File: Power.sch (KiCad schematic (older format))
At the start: 31 parts, among them J10 FAN, J8 PWR, Q1 AOD4189, Q10 MMBT3904, Q11 IRFML8244, Q2 AOD4189, Q8 MMBT3904, Q9 MMBT3906

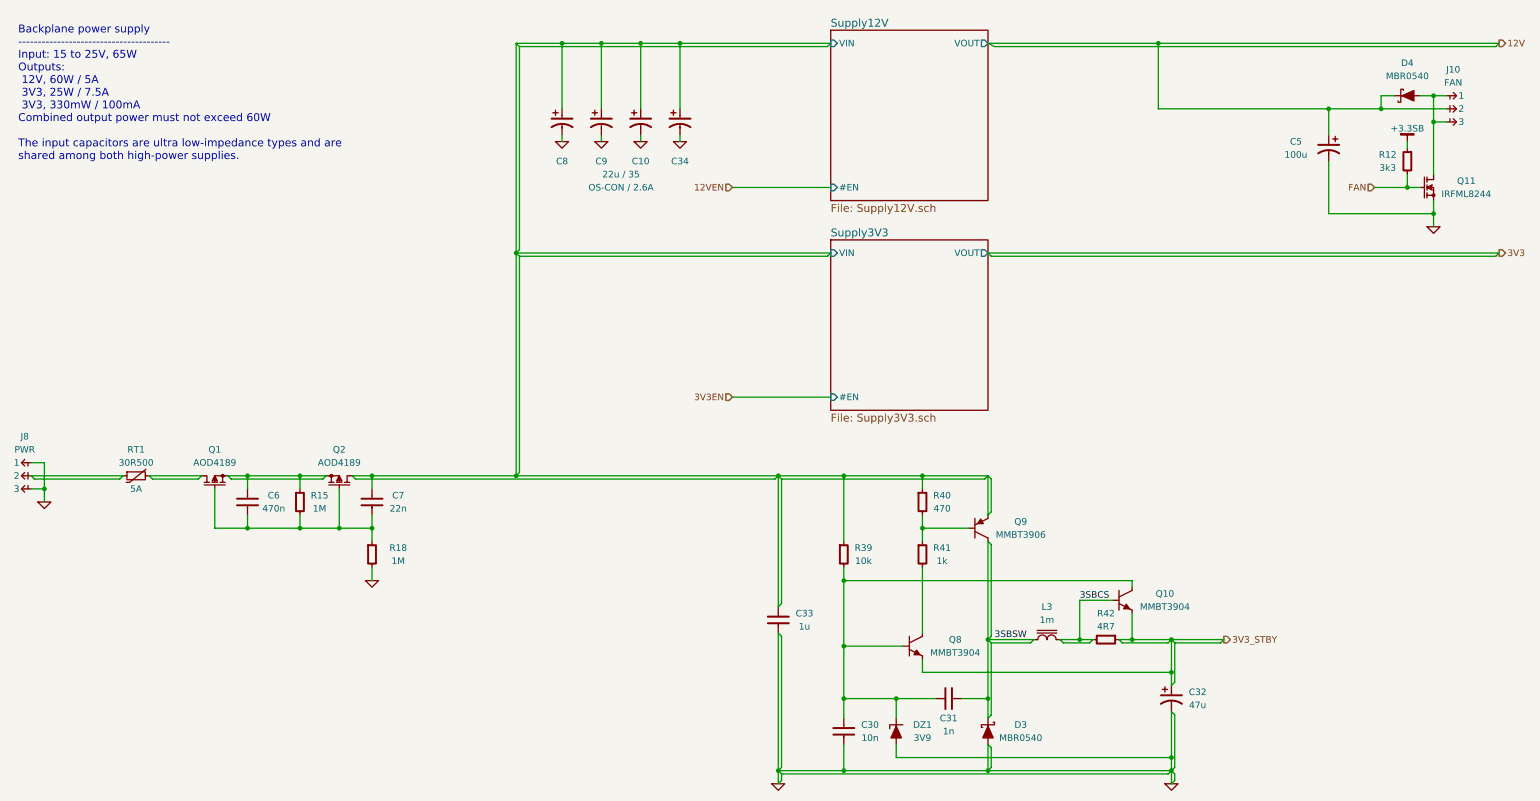
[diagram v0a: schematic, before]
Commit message: Reannotated parts
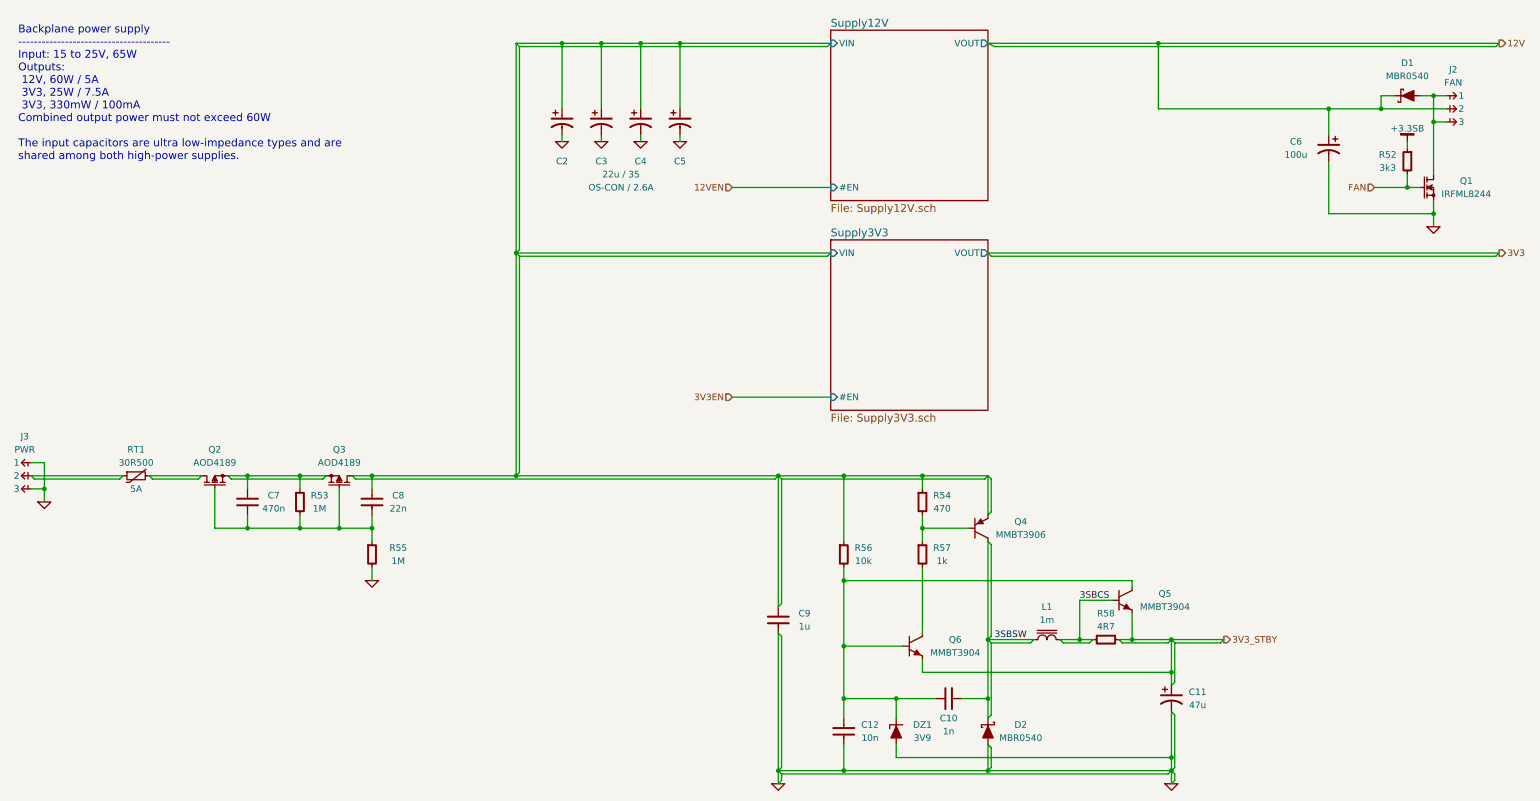
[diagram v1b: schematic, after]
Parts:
- renumbered C31 to C10, C32 to C11, C30 to C12, C8 to C2, C9 to C3, C10 to C4, C34 to C5, C5 to C6, C6 to C7, C7 to C8, C33 to C9, D4 to D1, D3 to D2, J10 to J2, J8 to J3, L3 to L1, Q11 to Q1, Q1 to Q2, Q2 to Q3, Q9 to Q4, Q10 to Q5, Q8 to Q6, R12 to R52, R15 to R53, R40 to R54, R18 to R55, R39 to R56, R41 to R57, R42 to R58

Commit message: Silkscreen and 3D touchups
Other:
- moved on the sheet: C10, C11, C12, C2, C3, C4, C5, C6, C7, C8, C9, D1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

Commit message: Changed BSS138 to MMUN221
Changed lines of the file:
@@
 $EndComp
 Wire Wire Line
-	7500 4600 7500 5350
-Wire Wire Line
-	7500 5350 7500 5800
-Wire Wire Line
-	7500 5800 7500 5950
+	7500 4600 7500 5950
 Wire Wire Line
 	7500 5350 7850 5350
@@
 	7350 4500 7000 4500
 Wire Wire Line
-	7000 4400 7000 4500
-Wire Wire Line
-	7000 4500 7000 4600
+	7000 4400 7000 4600
 Connection ~ 7000 4500
 Wire Wire Line
-	8050 5350 8200 5350
-Wire Wire Line
-	8200 5350 8300 5350
+	8050 5350 8300 5350
 Wire Wire Line
 	8600 5150 8600 5350
 Wire Wire Line
-	8500 5350 8600 5350
-Wire Wire Line
-	8600 5350 8900 5350
-Wire Wire Line
-	8900 5350 9300 5350
+	8500 5350 9300 5350
 Wire Wire Line
 	8200 5350 8200 5050
@@
 Connection ~ 8600 5350
 Wire Wire Line
-	8900 5350 8900 5600
-Wire Wire Line
-	8900 5600 8900 5700
-Wire Wire Line
-	8900 5900 8900 6250
-Wire Wire Line
-	8900 6250 8900 6350
-Wire Wire Line
-	8900 6350 8900 6450
+	8900 5350 8900 5700
+Wire Wire Line
+	8900 5900 8900 6450
 Wire Wire Line
 	7000 5500 7000 5600
@@
 Connection ~ 7500 5800
 Wire Wire Line
-	6400 4800 6400 4900
-Wire Wire Line
-	6400 4900 6400 5400
-Wire Wire Line
-	6400 5400 6400 5800
-Wire Wire Line
-	6400 5800 6400 5950
-Wire Wire Line
-	6400 5800 6800 5800
-Wire Wire Line
-	6800 5800 7100 5800
+	6400 4800 6400 5950
+Wire Wire Line
+	6400 5800 7100 5800
 Connection ~ 6400 5800
 Connection ~ 6400 5400
@@
 $EndComp
 Wire Wire Line
-	1950 4100 2100 4100
-Wire Wire Line
-	2100 4100 2500 4100
-Wire Wire Line
-	2500 4100 2700 4100
+	1950 4100 2700 4100
 $Comp
 L C-0805 C8
@@
 	3050 4100 3050 4200
 Wire Wire Line
-	3050 4400 3050 4500
-Wire Wire Line
-	3050 4500 3050 4600
-Wire Wire Line
-	1850 4500 2100 4500
-Wire Wire Line
-	2100 4500 2500 4500
-Wire Wire Line
-	2500 4500 2800 4500
-Wire Wire Line
-	2800 4500 3050 4500
+	3050 4400 3050 4600
+Wire Wire Line
+	1850 4500 3050 4500
 Wire Wire Line
 	2800 4500 2800 4200
@@
 $EndComp
 Wire Wire Line
-	5900 5300 5900 6350
-Wire Wire Line
-	5900 6350 5900 6450
+	5900 5300 5900 6450
 Text Label 7550 5350 0    50   ~ 0
 3SBSW
@@
 	800  4000 900  4000
 Wire Wire Line
-	900  4000 900  4200
-Wire Wire Line
-	900  4200 900  4300
+	900  4000 900  4300
 Wire Wire Line
 	900  4200 800  4200
@@
 $EndComp
 Wire Wire Line
-	9500 1200 9600 1200
-Wire Wire Line
-	9600 1200 9700 1200
-Wire Wire Line
-	9600 1200 9600 1400
-Wire Wire Line
-	9600 1400 9600 1800
+	9500 1200 9700 1200
+Wire Wire Line
+	9600 1200 9600 1800
 Wire Wire Line
 	9600 1400 9700 1400
@@
 $EndComp
 Wire Wire Line
-	9600 2000 9600 2100
-Wire Wire Line
-	9600 2100 9600 2200
+	9600 2000 9600 2200
 $Comp
 L R-0402 R52
@@
 	9400 1800 9400 1900
 Wire Wire Line
-	9150 1900 9400 1900
-Wire Wire Line
-	9400 1900 9500 1900
+	9150 1900 9500 1900
 $Comp
 L +3.3SB #PWR0211
@@
 $EndSheet
 Wire Wire Line
-	7500 1300 8800 1300
-Wire Wire Line
-	8800 1300 9200 1300
-Wire Wire Line
-	9200 1300 9700 1300
+	7500 1300 9700 1300
 Wire Wire Line
 	7500 1300 7500 800
 Wire Wire Line
-	7200 800  7500 800
-Wire Wire Line
-	7500 800  10100 800
+	7200 800  10100 800
 Connection ~ 7500 800
 Wire Wire Line
-	3700 4100 3700 2400
-Wire Wire Line
-	3700 2400 3700 800
+	3700 4100 3700 800
 $Comp
 L C-ALUM-6.3mm C2
@@
 $EndSheet
 Wire Wire Line
-	2900 4100 3050 4100
-Wire Wire Line
-	3050 4100 3700 4100
-Wire Wire Line
-	3700 4100 5900 4100
-Wire Wire Line
-	5900 4100 6400 4100
-Wire Wire Line
-	6400 4100 7000 4100
-Wire Wire Line
-	7000 4100 7500 4100
+	2900 4100 7500 4100
 Text HLabel 5250 3500 0    50   Input ~ 0
 3V3EN
@@
 Connection ~ 5900 4100
 Wire Wire Line
-	5900 6350 6400 6350
-Wire Wire Line
-	6400 6350 7500 6350
-Wire Wire Line
-	7500 6350 8900 6350
+	5900 6350 8900 6350
 $Comp
 L GND #PWR0216
@@
 	5925 6375 8875 6375
 Wire Wire Line
-	8875 6375 8900 6350
-Wire Wire Line
-	8900 6350 8925 6325
+	8875 6375 8925 6325
 Wire Wire Line
 	8900 6350 8925 6375
@@
 	5925 6325 5900 6350
 Wire Wire Line
-	3700 800  4050 800
-Wire Wire Line
-	4050 800  4350 800
-Wire Wire Line
-	4350 800  4650 800
-Wire Wire Line
-	4650 800  4950 800
-Wire Wire Line
-	4950 800  6000 800
+	3700 800  6000 800
 Connection ~ 4050 800
 Wire Wire Line

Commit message: Added power supply load test points
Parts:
- added TP1: 3V3, conn-test:TEST-PTH, symbol TESTPOINT
- added TP2: 12V, conn-test:TEST-PTH, symbol TESTPOINT
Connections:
- net 12V: now also TP2.1
- net 3V3: now also TP1.1
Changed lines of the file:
@@
 Text Notes 700  1700 0    60   ~ 0
 Backplane power supply\n---------------------------------------\nInput: 15 to 25V, 65W\nOutputs:\n 12V, 60W / 5A\n 3V3, 25W / 7.5A\n 3V3, 330mW / 100mA\nCombined output power must not exceed 60W\n\nThe input capacitors are ultra low-impedance types and are\nshared among both high-power supplies.
+$Comp
+L TESTPOINT TP2
+U 1 1 54D981B6
+P 7900 750
+F 0 "TP2" H 8050 900 50  0000 C CNN
+F 1 "12V" H 8050 800 50  0000 C CNN
+F 2 "conn-test:TEST-PTH" H 7900 750 50  0001 C CNN
+F 3 "" H 7900 750 50  0000 C CNN
+	1    7900 750
+	1    0    0    -1
+$EndComp
+Wire Wire Line
+	7900 750  7900 800
+Connection ~ 7900 800
+$Comp
+L TESTPOINT TP1
+U 1 1 54D98400
+P 7850 2350
+F 0 "TP1" H 8000 2500 50  0000 C CNN
+F 1 "3V3" H 8000 2400 50  0000 C CNN
+F 2 "conn-test:TEST-PTH" H 7850 2350 50  0001 C CNN
+F 3 "" H 7850 2350 50  0000 C CNN
+	1    7850 2350
+	1    0    0    -1
+$EndComp
+Wire Wire Line
+	7850 2350 7850 2400
+Connection ~ 7850 2400
 $EndSCHEMATC
